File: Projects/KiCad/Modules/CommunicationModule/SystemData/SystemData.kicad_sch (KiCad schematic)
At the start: 33 parts, among them J1 Conn_01x08, SW1 SW_DIP_x02, U1 MCP2562-E-P, U2 MCP2515-I/P, U3 NJM7805SDL1, U4 ABX00012, Y1 8MHz

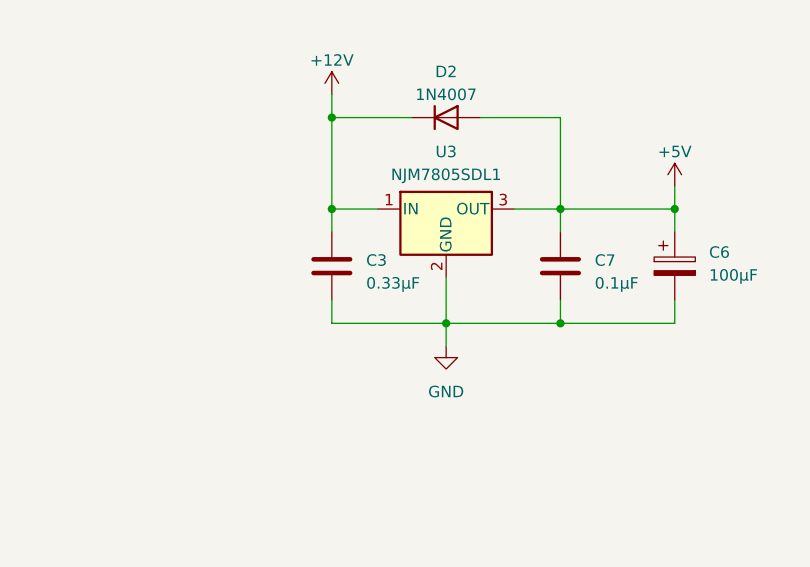
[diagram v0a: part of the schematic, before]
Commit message: チップ積層セラミックコンデンサをSMD1608に変更
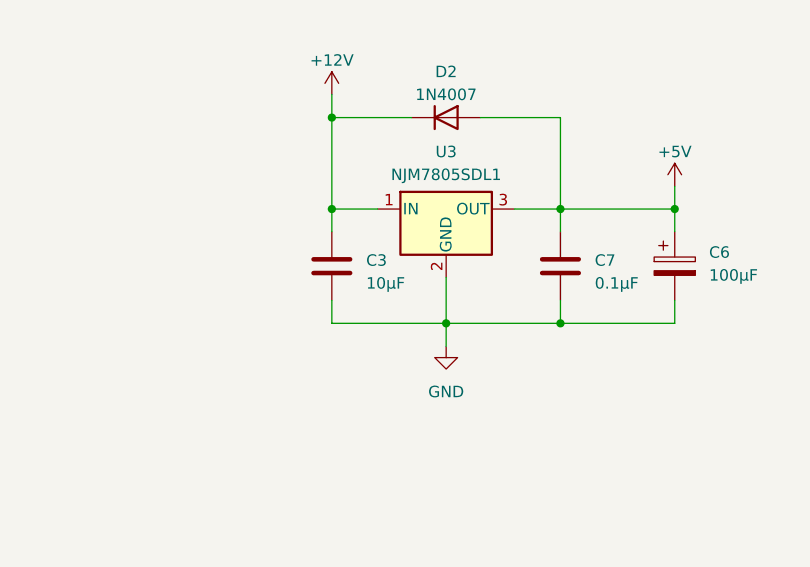
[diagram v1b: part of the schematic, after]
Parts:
- C2, C4, C5, C7: footprint Capacitor_SMD:C_0805_2012Metric_Pad1.18x1.45mm_HandSolder -> Capacitor_SMD:C_0603_1608Metric_Pad1.08x0.95mm_HandSolder
- C3: value 0.33μF -> 10μF; footprint Capacitor_SMD:C_0805_2012Metric_Pad1.18x1.45mm_HandSolder -> Capacitor_SMD:C_0603_1608Metric_Pad1.08x0.95mm_HandSolder
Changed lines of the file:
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@@
       (effects (font (size 1.27 1.27)) (justify left))
     )
-    (property "Footprint" "Capacitor_SMD:C_0805_2012Metric_Pad1.18x1.45mm_HandSolder" (at 97.4852 35.56 0)
+    (property "Footprint" "Capacitor_SMD:C_0603_1608Metric_Pad1.08x0.95mm_HandSolder" (at 97.4852 35.56 0)
       (effects (font (size 1.27 1.27)) hide)
     )
@@
       (effects (font (size 1.27 1.27)) (justify left))
     )
-    (property "Footprint" "Capacitor_SMD:C_0805_2012Metric_Pad1.18x1.45mm_HandSolder" (at 150.8252 30.48 0)
+    (property "Footprint" "Capacitor_SMD:C_0603_1608Metric_Pad1.08x0.95mm_HandSolder" (at 150.8252 30.48 0)
       (effects (font (size 1.27 1.27)) hide)
     )
@@
       (effects (font (size 1.27 1.27)) (justify left))
     )
-    (property "Footprint" "Capacitor_SMD:C_0805_2012Metric_Pad1.18x1.45mm_HandSolder" (at 88.5952 35.56 0)
+    (property "Footprint" "Capacitor_SMD:C_0603_1608Metric_Pad1.08x0.95mm_HandSolder" (at 88.5952 35.56 0)
       (effects (font (size 1.27 1.27)) hide)
     )
@@
       (effects (font (size 1.27 1.27)) (justify left))
     )
-    (property "Value" "0.33μF" (at 215.9 108.585 0)
-      (effects (font (size 1.27 1.27)) (justify left))
-    )
-    (property "Footprint" "Capacitor_SMD:C_0805_2012Metric_Pad1.18x1.45mm_HandSolder" (at 213.0552 110.49 0)
+    (property "Value" "10μF" (at 215.9 108.585 0)
+      (effects (font (size 1.27 1.27)) (justify left))
+    )
+    (property "Footprint" "Capacitor_SMD:C_0603_1608Metric_Pad1.08x0.95mm_HandSolder" (at 213.0552 110.49 0)
       (effects (font (size 1.27 1.27)) hide)
     )
@@
       (effects (font (size 1.27 1.27)) (justify left))
     )
-    (property "Footprint" "Capacitor_SMD:C_0805_2012Metric_Pad1.18x1.45mm_HandSolder" (at 238.4552 110.49 0)
-      (effects (font (size 1.27 1.27)) hide)
-    )
+    (property "Footprint" "Capacitor_SMD:C_0603_1608Metric_Pad1.08x0.95mm_HandSolder" (at 238.4552 110.49 0)
+      (effects (font (size 1.27 1.27)) hide)
+    )

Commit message: 抵抗の在庫に合わせてサイズを変更
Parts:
- R3, R4, R5, R6, R7: footprint Resistor_SMD:R_0603_1608Metric_Pad0.98x0.95mm_HandSolder -> Resistor_SMD:R_0805_2012Metric_Pad1.20x1.40mm_HandSolder
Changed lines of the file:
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@@
       (effects (font (size 1.27 1.27)))
     )
-    (property "Footprint" "Resistor_SMD:R_0603_1608Metric_Pad0.98x0.95mm_HandSolder" (at 156.21 70.358 90)
+    (property "Footprint" "Resistor_SMD:R_0805_2012Metric_Pad1.20x1.40mm_HandSolder" (at 156.21 70.358 90)
       (effects (font (size 1.27 1.27)) hide)
     )
@@
       (effects (font (size 1.27 1.27)) (justify left))
     )
-    (property "Footprint" "Resistor_SMD:R_0603_1608Metric_Pad0.98x0.95mm_HandSolder" (at 54.102 167.64 90)
+    (property "Footprint" "Resistor_SMD:R_0805_2012Metric_Pad1.20x1.40mm_HandSolder" (at 54.102 167.64 90)
       (effects (font (size 1.27 1.27)) hide)
     )
@@
       (effects (font (size 1.27 1.27)) (justify left))
     )
-    (property "Footprint" "Resistor_SMD:R_0603_1608Metric_Pad0.98x0.95mm_HandSolder" (at 64.262 167.64 90)
+    (property "Footprint" "Resistor_SMD:R_0805_2012Metric_Pad1.20x1.40mm_HandSolder" (at 64.262 167.64 90)
       (effects (font (size 1.27 1.27)) hide)
     )
@@
       (effects (font (size 1.27 1.27)) (justify left))
     )
-    (property "Footprint" "Resistor_SMD:R_0603_1608Metric_Pad0.98x0.95mm_HandSolder" (at 74.422 167.64 90)
+    (property "Footprint" "Resistor_SMD:R_0805_2012Metric_Pad1.20x1.40mm_HandSolder" (at 74.422 167.64 90)
       (effects (font (size 1.27 1.27)) hide)
     )
@@
       (effects (font (size 1.27 1.27)) (justify left))
     )
-    (property "Footprint" "Resistor_SMD:R_0603_1608Metric_Pad0.98x0.95mm_HandSolder" (at 84.582 167.64 90)
-      (effects (font (size 1.27 1.27)) hide)
-    )
+    (property "Footprint" "Resistor_SMD:R_0805_2012Metric_Pad1.20x1.40mm_HandSolder" (at 84.582 167.64 90)
+      (effects (font (size 1.27 1.27)) hide)
+    )

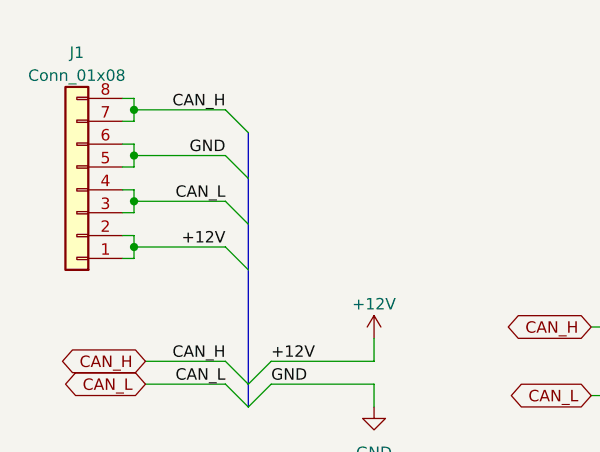
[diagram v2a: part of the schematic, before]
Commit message: コネクタのピン配置を変更
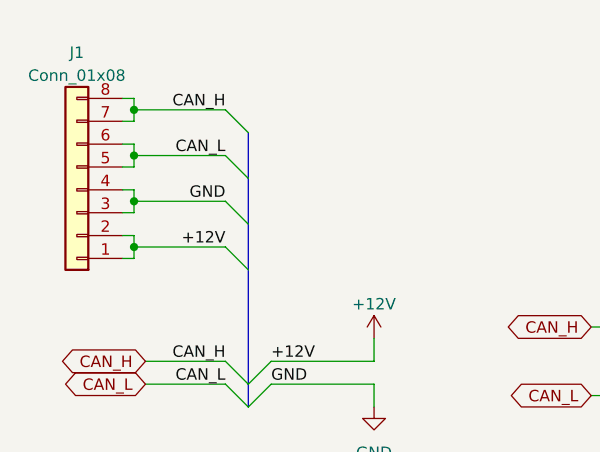
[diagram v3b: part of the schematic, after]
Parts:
- J1: footprint Connector_Hirose:Hirose_DF11-8DP-2DSA_2x04_P2.00mm_Vertical -> Hirose_Connector:Hirose_DF11B-8DP-2DS
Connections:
- net CAN_L: now also J1.5 (Pin_5), J1.6 (Pin_6); no longer J1.3 (Pin_3), J1.4 (Pin_4)
- net GND: now also J1.3 (Pin_3), J1.4 (Pin_4); no longer J1.5 (Pin_5), J1.6 (Pin_6)
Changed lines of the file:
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@@
+    (effects (font (size 1.27 1.27)) (justify right bottom))
+  )
+  (label "GND" (at 39.37 35.56 180) (fields_autoplaced)
     (effects (font (size 1.27 1.27)) (justify right bottom))
   )
@@
     (effects (font (size 1.27 1.27)) (justify left bottom))
   )
-  (label "GND" (at 39.37 30.48 180) (fields_autoplaced)
-    (effects (font (size 1.27 1.27)) (justify right bottom))
-  )
-  (label "CAN_L" (at 39.37 35.56 180) (fields_autoplaced)
+  (label "CAN_L" (at 39.37 30.48 180) (fields_autoplaced)
     (effects (font (size 1.27 1.27)) (justify right bottom))
   )
@@
       (effects (font (size 1.27 1.27)))
     )
-    (property "Footprint" "Connector_Hirose:Hirose_DF11-8DP-2DSA_2x04_P2.00mm_Vertical" (at 22.86 34.29 0)
-      (effects (font (size 1.27 1.27)) hide)
-    )
+    (property "Footprint" "Hirose_Connector:Hirose_DF11B-8DP-2DS" (at 22.86 34.29 0)
+      (effects (font (size 1.27 1.27)) hide)
+    )

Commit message: クリスタルをSMDに変更
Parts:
- Y1: footprint Crystal:Crystal_HC49-U_Vertical -> Crystal:Crystal_SMD_HC49-SD
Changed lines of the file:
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@@
       (effects (font (size 1.27 1.27)) (justify right))
     )
-    (property "Footprint" "Crystal:Crystal_HC49-U_Vertical" (at 257.81 33.02 0)
+    (property "Footprint" "Crystal:Crystal_SMD_HC49-SD" (at 257.81 33.02 0)
       (effects (font (size 1.27 1.27)) hide)
     )

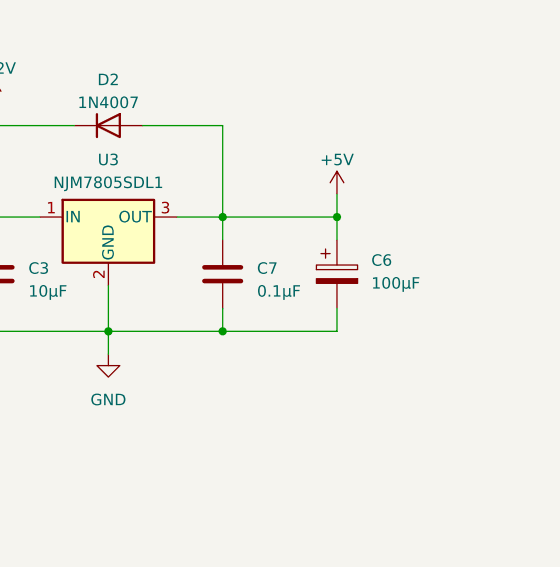
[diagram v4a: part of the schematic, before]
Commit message: バッファコンデンサを表面実装に変更
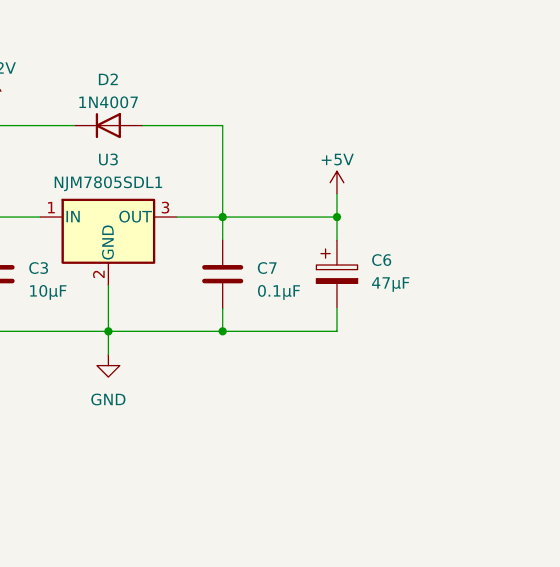
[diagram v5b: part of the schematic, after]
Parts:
- C6: value 100μF -> 47μF; footprint Capacitor_SMD:CP_Elec_6.3x7.7 -> Capacitor_SMD:CP_Elec_6.3x5.9
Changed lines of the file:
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@@
       (effects (font (size 1.27 1.27)) (justify left))
     )
-    (property "Value" "100μF" (at 254 107.696 0)
+    (property "Value" "47μF" (at 254 107.696 0)
       (effects (font (size 1.27 1.27)) (justify left))
     )
-    (property "Footprint" "Capacitor_SMD:CP_Elec_6.3x7.7" (at 251.1552 110.49 0)
+    (property "Footprint" "Capacitor_SMD:CP_Elec_6.3x5.9" (at 251.1552 110.49 0)
       (effects (font (size 1.27 1.27)) hide)
     )

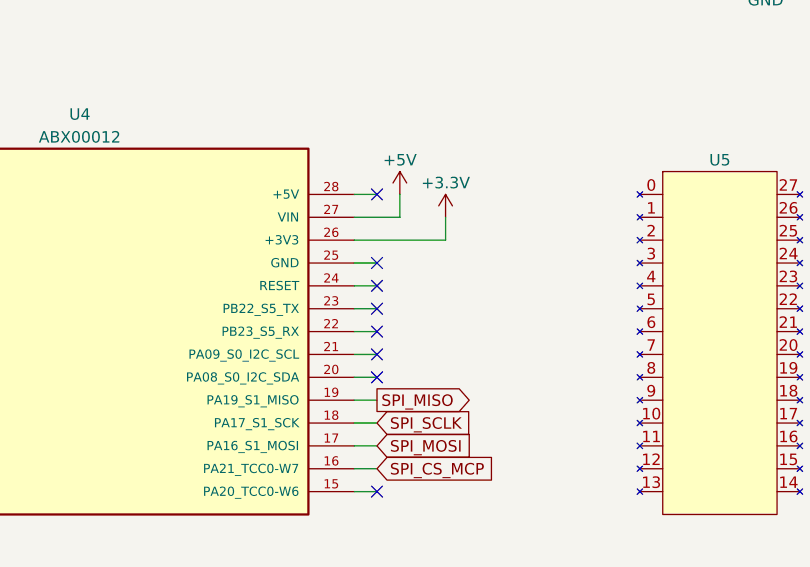
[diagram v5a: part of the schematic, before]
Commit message: 配線の繋ぎ忘れを修正
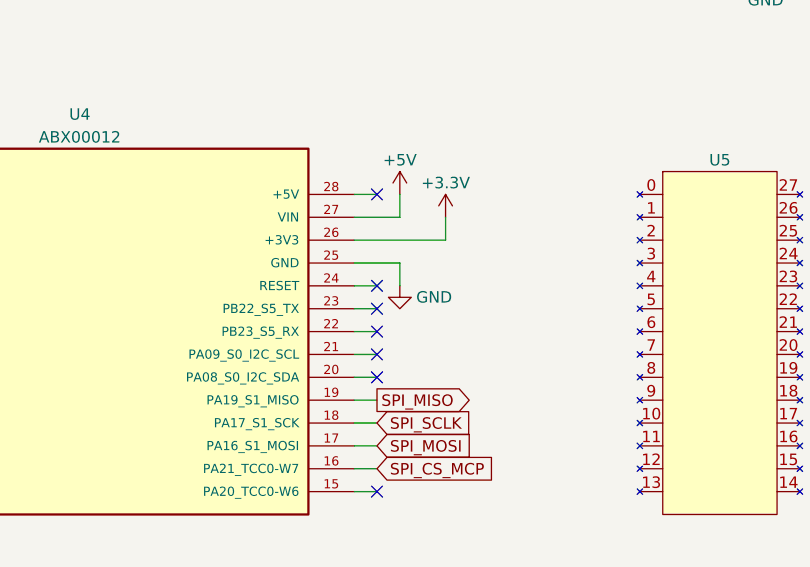
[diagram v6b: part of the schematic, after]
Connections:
- net GND: now also U4.25 (GND)
- no-connect marks 16 -> 15
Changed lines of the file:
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@@
   (no_connect (at 123.19 95.25))
   (no_connect (at 57.15 105.41))
-  (no_connect (at 123.19 102.87))
   (no_connect (at 57.15 110.49))
   (no_connect (at 57.15 95.25))
@@
     (stroke (width 0) (type default))
   )
-  (wire (pts (xy 120.65 102.87) (xy 123.19 102.87))
+  (wire (pts (xy 120.65 102.87) (xy 125.73 102.87))
     (stroke (width 0) (type default))
   )
@@
   )
   (wire (pts (xy 217.17 100.33) (xy 212.09 100.33))
+    (stroke (width 0) (type default))
+  )
+  (wire (pts (xy 125.73 102.87) (xy 125.73 105.41))
     (stroke (width 0) (type default))
   )
@@
         )
       )
+    )
+  )
+  (symbol (lib_id "power:GND") (at 125.73 105.41 0) (unit 1)
+    (in_bom yes) (on_board yes) (dnp no)
+    (property "Reference" "#PWR030" (at 125.73 111.76 0)
+      (effects (font (size 1.27 1.27)) hide)
+    )
+    (property "Value" "GND" (at 129.54 106.68 0)
+      (effects (font (size 1.27 1.27)))
+    )
+    (property "Footprint" "" (at 125.73 105.41 0)
+      (effects (font (size 1.27 1.27)) hide)
+    )
+    (property "Datasheet" "" (at 125.73 105.41 0)
+      (effects (font (size 1.27 1.27)) hide)
+    )
+    (pin "1")
+    (instances
+      (project "SystemData"
+        (path "/ea1ed597-7cd3-4340-902e-bdce8f2d7a62"
+          (reference "#PWR030") (unit 1)
+        )
+      )

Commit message: ガーバーを再生成
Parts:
- C2, C4, C5, C7: value 0.1μF -> 0.1uF
- C3: value 10μF -> 10uF
- C6: value 47μF -> 47uF
- D3, D4, D5, D6: value ORANGE -> BLUE
- R1: value 120Ω -> 120R
- R2: value 620Ω -> 620R
- R3: value 10kΩ -> 10kR
- R4, R5, R6, R7: value 100Ω -> 100R
- R8: value 300Ω -> 300R
- U5: value ~ -> ASX00017
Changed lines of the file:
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@@
       (effects (font (size 1.27 1.27)) (justify left))
     )
-    (property "Value" "300Ω" (at 99.06 168.9099 0)
+    (property "Value" "300R" (at 99.06 168.9099 0)
       (effects (font (size 1.27 1.27)) (justify left))
     )
@@
       (effects (font (size 1.27 1.27)))
     )
-    (property "Value" "10kΩ" (at 156.21 66.04 90)
+    (property "Value" "10kR" (at 156.21 66.04 90)
       (effects (font (size 1.27 1.27)))
     )
@@
       (effects (font (size 1.27 1.27)))
     )
-    (property "Value" "~" (at 154.94 91.44 0)
+    (property "Value" "ASX00017" (at 154.94 91.44 0)
       (effects (font (size 1.27 1.27)))
     )
@@
       (effects (font (size 1.27 1.27)) (justify left))
     )
-    (property "Value" "620Ω" (at 49.53 168.9099 0)
+    (property "Value" "620R" (at 49.53 168.9099 0)
       (effects (font (size 1.27 1.27)) (justify left))
     )
@@
       (effects (font (size 1.27 1.27)) (justify left))
     )
-    (property "Value" "0.1μF" (at 99.06 33.02 0)
+    (property "Value" "0.1uF" (at 99.06 33.02 0)
       (effects (font (size 1.27 1.27)) (justify left))
     )
@@
       (effects (font (size 1.27 1.27)) (justify left))
     )
-    (property "Value" "0.1μF" (at 152.4 27.94 0)
+    (property "Value" "0.1uF" (at 152.4 27.94 0)
       (effects (font (size 1.27 1.27)) (justify left))
     )
@@
       (effects (font (size 1.27 1.27)) (justify left))
     )
-    (property "Value" "0.1μF" (at 90.17 33.02 0)
+    (property "Value" "0.1uF" (at 90.17 33.02 0)
       (effects (font (size 1.27 1.27)) (justify left))
     )
@@
       (effects (font (size 1.27 1.27)) (justify left))
     )
-    (property "Value" "100Ω" (at 58.42 168.9099 0)
+    (property "Value" "100R" (at 58.42 168.9099 0)
       (effects (font (size 1.27 1.27)) (justify left))
     )
@@
       (effects (font (size 1.27 1.27)) (justify right))
     )
-    (property "Value" "ORANGE" (at 69.85 180.6574 90)
+    (property "Value" "BLUE" (at 69.85 180.6574 90)
       (effects (font (size 1.27 1.27)) (justify right))
     )
@@
       (effects (font (size 1.27 1.27)) (justify left))
     )
-    (property "Value" "47μF" (at 254 107.696 0)
+    (property "Value" "47uF" (at 254 107.696 0)
       (effects (font (size 1.27 1.27)) (justify left))
     )
@@
       (effects (font (size 1.27 1.27)) (justify left))
     )
-    (property "Value" "10μF" (at 215.9 108.585 0)
+    (property "Value" "10uF" (at 215.9 108.585 0)
       (effects (font (size 1.27 1.27)) (justify left))
     )
@@
       (effects (font (size 1.27 1.27)) (justify right))
     )
-    (property "Value" "ORANGE" (at 90.17 180.6574 90)
+    (property "Value" "BLUE" (at 90.17 180.6574 90)
       (effects (font (size 1.27 1.27)) (justify right))
     )
@@
       (effects (font (size 1.27 1.27)) (justify left))
     )
-    (property "Value" "100Ω" (at 68.58 168.9099 0)
+    (property "Value" "100R" (at 68.58 168.9099 0)
       (effects (font (size 1.27 1.27)) (justify left))
     )
@@
       (effects (font (size 1.27 1.27)) (justify right))
     )
-    (property "Value" "ORANGE" (at 59.69 180.6574 90)
+    (property "Value" "BLUE" (at 59.69 180.6574 90)
       (effects (font (size 1.27 1.27)) (justify right))
     )
@@
       (effects (font (size 1.27 1.27)) (justify left))
     )
-    (property "Value" "100Ω" (at 78.74 168.9099 0)
+    (property "Value" "100R" (at 78.74 168.9099 0)
       (effects (font (size 1.27 1.27)) (justify left))
     )
@@
       (effects (font (size 1.27 1.27)) (justify right))
     )
-    (property "Value" "ORANGE" (at 80.01 180.6574 90)
+    (property "Value" "BLUE" (at 80.01 180.6574 90)
       (effects (font (size 1.27 1.27)) (justify right))
     )
@@
       (effects (font (size 1.27 1.27)) (justify left))
     )
-    (property "Value" "100Ω" (at 88.9 168.9099 0)
+    (property "Value" "100R" (at 88.9 168.9099 0)
       (effects (font (size 1.27 1.27)) (justify left))
     )
@@
       (effects (font (size 1.27 1.27)) (justify left))
     )
-    (property "Value" "120Ω" (at 85.09 54.61 0)
+    (property "Value" "120R" (at 85.09 54.61 0)
       (effects (font (size 1.27 1.27)) (justify left))
     )
@@
       (effects (font (size 1.27 1.27)) (justify left))
     )
-    (property "Value" "0.1μF" (at 241.3 108.585 0)
-      (effects (font (size 1.27 1.27)) (justify left))
-    )
+    (property "Value" "0.1uF" (at 241.3 108.585 0)
+      (effects (font (size 1.27 1.27)) (justify left))
+    )
